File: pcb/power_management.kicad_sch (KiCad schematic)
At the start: 13 parts, among them U4 LMR51430XDDCR

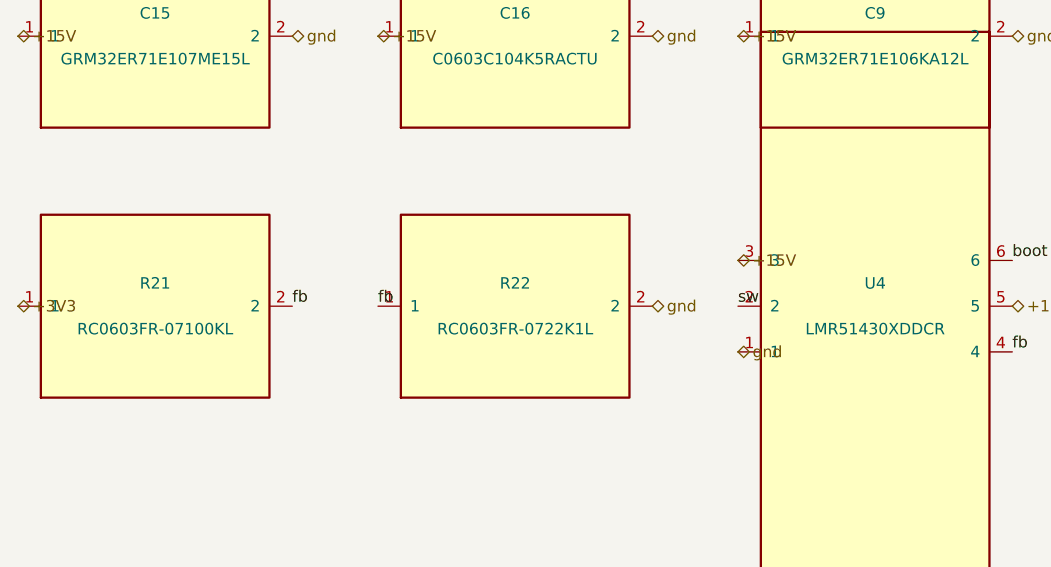
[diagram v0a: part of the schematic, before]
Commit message: fix(pcb): regenerate stale schematic against current elec/src (spike)
pcb/temper.kicad_sch was last regenerated 2026-08-03; elec/src gained the
OCP-02 second-CT module and J_RTD1 pan-probe connector (2026-08-07/08-08)
and lost the ZCD-opto circuit (2026-08-07) without a schematic resync,
leaving scripts/check_erc_off_grid_consequence.py red with 86 MISMATCH
findings on unmodified code.

Diagnosis (docs/evidence/2026-08-11-schematic-elec-drift.md): 81 of the 86
are pure designator-identity churn from the same RENUMBERED cascade
check_netlist_board_reconciliation.py already reports independently (same
physical nets, different (ref,pin) labels); 5 are nets the stale drawing
never had at all (the new OCP-02/pan-probe circuitry). Zero net names that
today's netclass work depends on (ac_l, ac_n, gnd, +170V_BUS, SW_NODE,
GATE_HS/LS, RTD/SPI) were added, removed, or renamed.

Regenerated pcb/*.kicad_sch only (oracle-verified isomorphic to
elec/build/default.net; ERC ratchet still passes at 495<=498 warnings,
0 errors; off-grid-consequence gate 86->1, the residual being a genuine
single-pin net (ac_l) exposed by the ZCD deletion, not a new defect).

The board (pcb/temper.kicad_pcb) is untouched and remains out of sync
with elec/src independently of this fix -- neither caused nor cured by a
schematic regen, since no board-facing gate reads the schematic. 125
reconciliation findings / 13 footprint-drift findings persist unchanged:
6 components (J1, C37, U19, T2, R65, TP3) need board placement and 7
stale ZCD-circuit components (D2, R6-R10, U3) need removal, on a board
currently 0/110 routed. That is a CP-SAT placement decision for the
board owner, not attempted here.

Co-Authored-By: Claude Opus 5 (1M context) <noreply@anthropic.com>
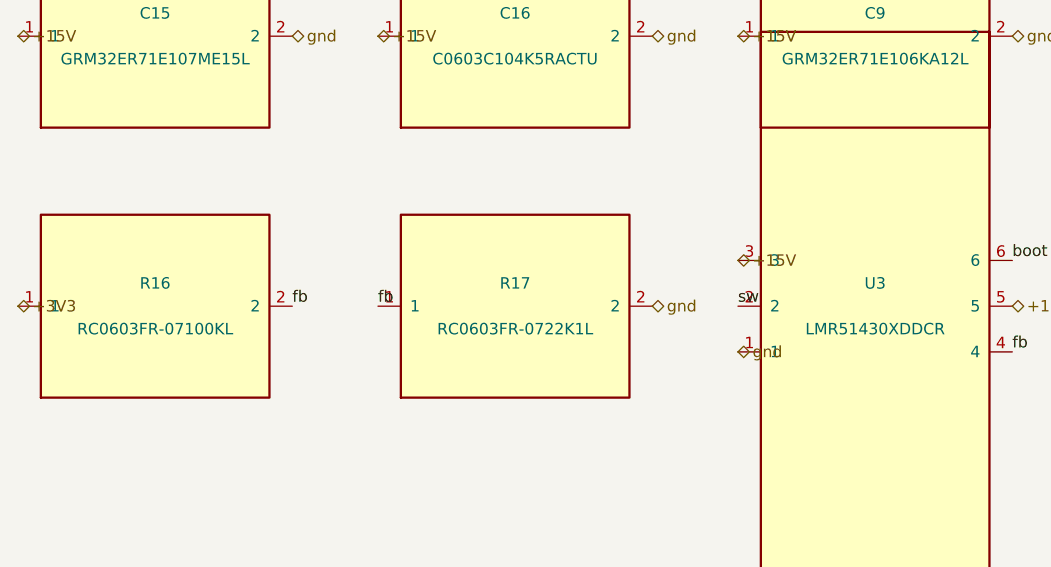
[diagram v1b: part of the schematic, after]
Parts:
- R16: renamed from R21; symbol RC0603FR-0710KL -> RC0603FR-07100KL
- R17: renamed from R22; symbol RC0603FR-0710KL -> RC0603FR-07100KL
- renumbered U4 to U3
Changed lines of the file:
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@@
   )
   (symbol
-    (lib_id "RC0603FR-0710KL")
+    (lib_id "RC0603FR-07100KL")
     (at 50.80 110.80 0)
     (unit 1)
@@
     (on_board yes)
     (dnp no)
-    (property "Reference" "R21" (at 50.80 108.26 0) (effects (font (size 1.27 1.27))))
+    (property "Reference" "R16" (at 50.80 108.26 0) (effects (font (size 1.27 1.27))))
     (property "Value" "RC0603FR-07100KL" (at 50.80 113.34 0) (effects (font (size 1.27 1.27))))
     (property "Footprint" "Resistor_SMD:R_0603_1608Metric" (at 50.80 110.80 0) (effects (font (size 1.27 1.27)) hide))
@@
   )
   (symbol
-    (lib_id "RC0603FR-0710KL")
+    (lib_id "RC0603FR-07100KL")
     (at 90.80 110.80 0)
     (unit 1)
@@
     (on_board yes)
     (dnp no)
-    (property "Reference" "R22" (at 90.80 108.26 0) (effects (font (size 1.27 1.27))))
+    (property "Reference" "R17" (at 90.80 108.26 0) (effects (font (size 1.27 1.27))))
     (property "Value" "RC0603FR-0722K1L" (at 90.80 113.34 0) (effects (font (size 1.27 1.27))))
     (property "Footprint" "Resistor_SMD:R_0603_1608Metric" (at 90.80 110.80 0) (effects (font (size 1.27 1.27)) hide))
@@
     (on_board yes)
     (dnp no)
-    (property "Reference" "U4" (at 130.80 108.26 0) (effects (font (size 1.27 1.27))))
+    (property "Reference" "U3" (at 130.80 108.26 0) (effects (font (size 1.27 1.27))))
     (property "Value" "LMR51430XDDCR" (at 130.80 113.34 0) (effects (font (size 1.27 1.27))))
     (property "Footprint" "Package_TO_SOT_SMD:SOT-23-6" (at 130.80 110.80 0) (effects (font (size 1.27 1.27)) hide))
